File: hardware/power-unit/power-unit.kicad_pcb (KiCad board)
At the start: 2 copper layers, 114 x 80 mm, 19 parts, among them J1 VCC, J2 PWR Switch, J3 5V out, J4 Rear LED data, J5 LED left, J6 LED right, K1 G5LE-1

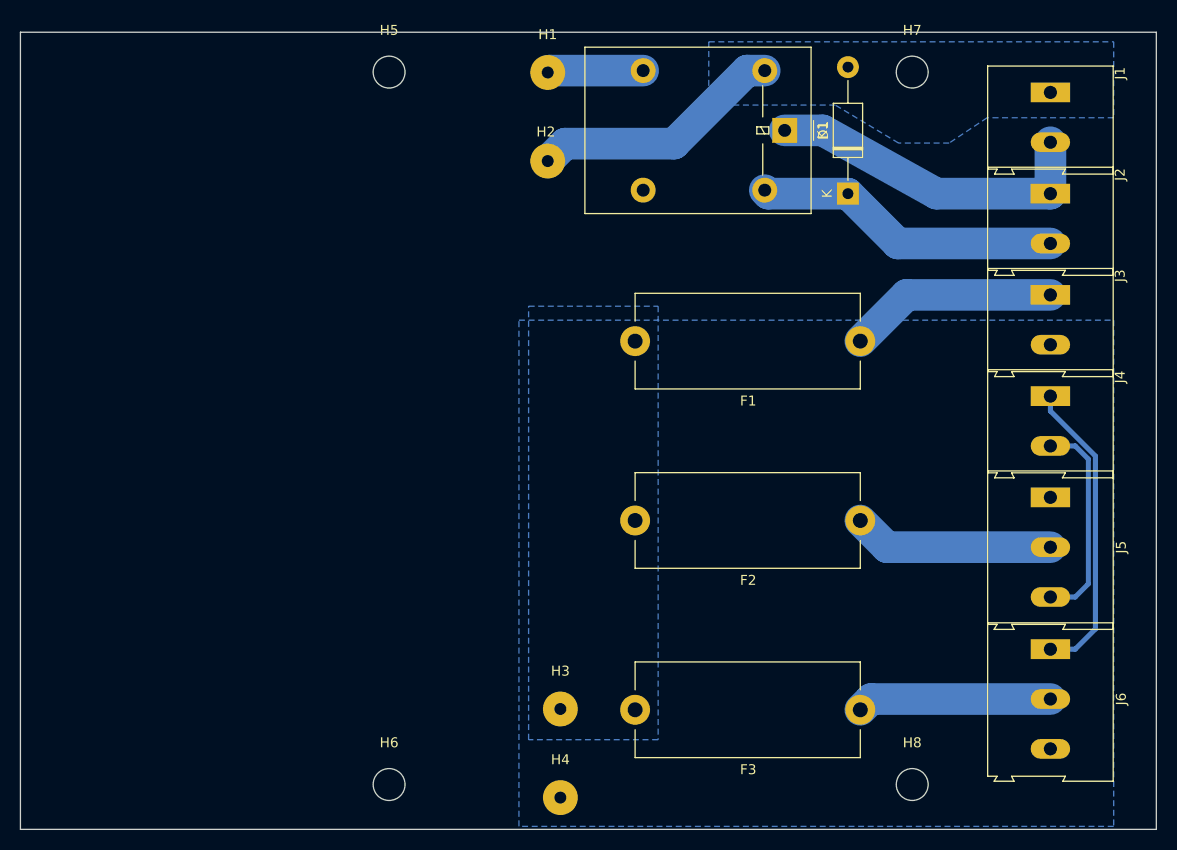
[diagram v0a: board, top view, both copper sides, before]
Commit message: Update power unit pcb
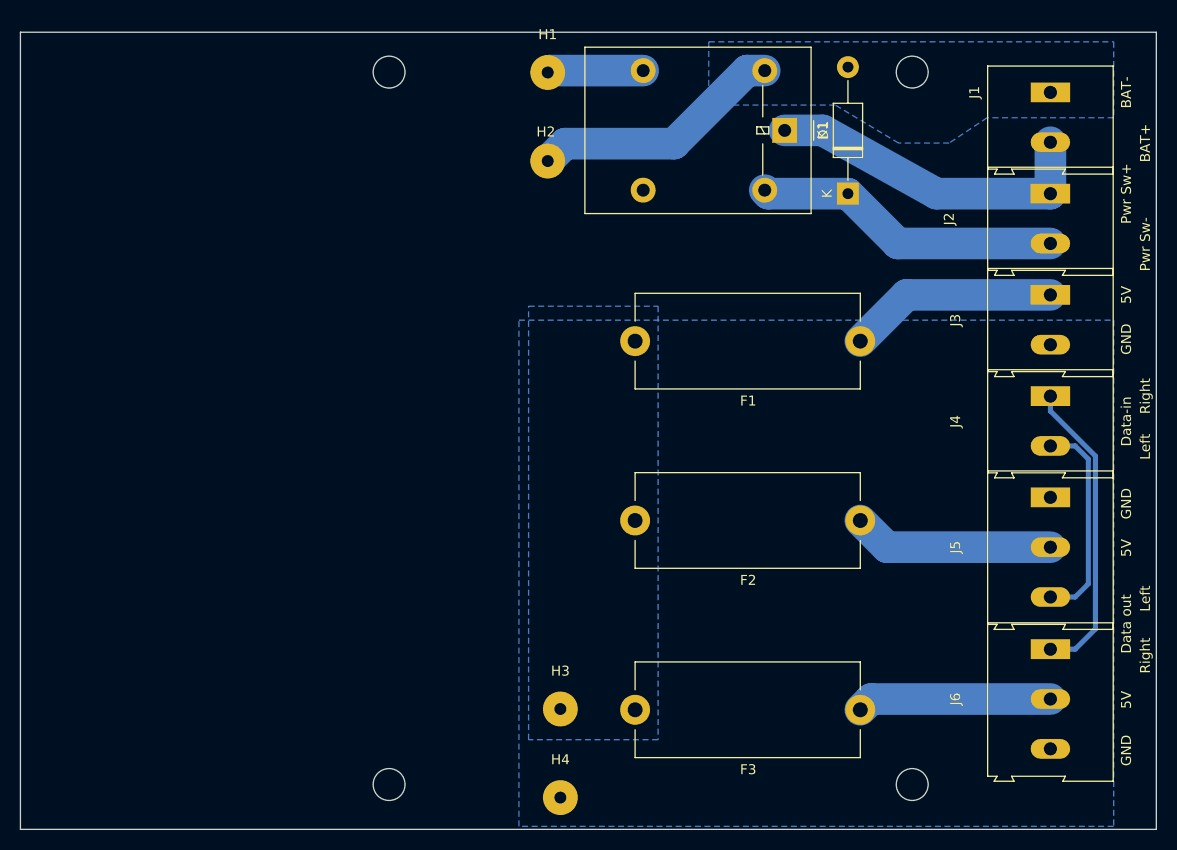
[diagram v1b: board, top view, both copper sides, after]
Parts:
- J1: value VCC -> VCC 12V
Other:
- board text added: "5V"
- board text added: "BAT+"
- board text added: "BAT-"
- board text added: "Data out"
- board text added: "Data-in"
- board text added: "GND"
- board text added: "Left"
- board text added: "Pwr Sw+"
- board text added: "Pwr Sw-"
- board text added: "Right"
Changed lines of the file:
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@@
   (general
     (thickness 1.6)
-    (drawings 16)
+    (drawings 32)
     (tracks 30)
     (zones 0)
@@
   )
   (setup
-    (last_trace_width 0.508)
+    (last_trace_width 0.25)
     (user_trace_width 0.508)
     (user_trace_width 3.175)
@@
     (visible_elements 7FFFEFFF)
     (pcbplotparams
-      (layerselection 0x010fc_ffffffff)
+      (layerselection 0x21060_fffffffe)
       (usegerberextensions false)
       (usegerberattributes false)
       (usegerberadvancedattributes false)
       (creategerberjobfile false)
-      (excludeedgelayer true)
+      (excludeedgelayer false)
       (linewidth 0.100000)
       (plotframeref false)
@@
       (padsonsilk false)
       (subtractmaskfromsilk false)
-      (outputformat 1)
+      (outputformat 4)
       (mirror false)
-      (drillshape 1)
+      (drillshape 2)
       (scaleselection 1)
-      (outputdirectory ""))
+      (outputdirectory "c:/Users/gohol/OneDrive/Documents/Cargo bike lights/power-unit/"))
   )
   (net 0 "")
@@
     (clearance 2.032)
     (attr virtual)
-    (fp_text reference H8 (at 0 -4.2) (layer F.SilkS)
-      (effects (font (size 1 1) (thickness 0.15)))
-    )
-    (fp_text value MountingHole (at 0 4.2) (layer F.Fab)
+    (fp_text reference H8 (at 0 -4.2) (layer F.SilkS) hide
+      (effects (font (size 1 1) (thickness 0.15)))
+    )
+    (fp_text value MountingHole (at 0 4.2) (layer F.Fab) hide
       (effects (font (size 1 1) (thickness 0.15)))
     )
@@
     (clearance 2.54)
     (attr virtual)
-    (fp_text reference H7 (at 0 -4.2) (layer F.SilkS)
-      (effects (font (size 1 1) (thickness 0.15)))
-    )
-    (fp_text value MountingHole (at 0 4.2) (layer F.Fab)
+    (fp_text reference H7 (at 0 -4.2) (layer F.SilkS) hide
+      (effects (font (size 1 1) (thickness 0.15)))
+    )
+    (fp_text value MountingHole (at 0 4.2) (layer F.Fab) hide
       (effects (font (size 1 1) (thickness 0.15)))
     )
@@
     (tags "mounting hole 3.2mm no annular m3")
     (attr virtual)
-    (fp_text reference H6 (at 0 -4.2) (layer F.SilkS)
-      (effects (font (size 1 1) (thickness 0.15)))
-    )
-    (fp_text value MountingHole (at 0 4.2) (layer F.Fab)
+    (fp_text reference H6 (at 0 -4.2) (layer F.SilkS) hide
+      (effects (font (size 1 1) (thickness 0.15)))
+    )
+    (fp_text value MountingHole (at 0 4.2) (layer F.Fab) hide
       (effects (font (size 1 1) (thickness 0.15)))
     )
@@
     (tags "mounting hole 3.2mm no annular m3")
     (attr virtual)
-    (fp_text reference H5 (at 0 -4.2) (layer F.SilkS)
-      (effects (font (size 1 1) (thickness 0.15)))
-    )
-    (fp_text value MountingHole (at 0 4.2) (layer F.Fab)
+    (fp_text reference H5 (at 0 -4.2) (layer F.SilkS) hide
+      (effects (font (size 1 1) (thickness 0.15)))
+    )
+    (fp_text value MountingHole (at 0 4.2) (layer F.Fab) hide
       (effects (font (size 1 1) (thickness 0.15)))
     )
@@
     (descr "Altech AK300 terminal block, pitch 5.0mm, 45 degree angled, see http://www.mouser.com/ds/2/16/PCBMETRC-24178.pdf")
     (tags "Altech AK300 terminal block pitch 5.0mm")
-    (fp_text reference J1 (at -1.92 -6.99 90) (layer F.SilkS)
-      (effects (font (size 1 1) (thickness 0.15)))
-    )
-    (fp_text value VCC (at 2.78 7.75 90) (layer F.Fab)
+    (fp_text reference J1 (at 0 7.62 90) (layer F.SilkS)
+      (effects (font (size 1 1) (thickness 0.15)))
+    )
+    (fp_text value "VCC 12V" (at 2.78 7.75 90) (layer F.Fab)
       (effects (font (size 1 1) (thickness 0.15)))
     )
@@
     (descr "Altech AK300 terminal block, pitch 5.0mm, 45 degree angled, see http://www.mouser.com/ds/2/16/PCBMETRC-24178.pdf")
     (tags "Altech AK300 terminal block pitch 5.0mm")
-    (fp_text reference J2 (at -1.92 -6.99 90) (layer F.SilkS)
+    (fp_text reference J2 (at 2.54 10.16 90) (layer F.SilkS)
       (effects (font (size 1 1) (thickness 0.15)))
     )
@@
     (descr "Altech AK300 terminal block, pitch 5.0mm, 45 degree angled, see http://www.mouser.com/ds/2/16/PCBMETRC-24178.pdf")
     (tags "Altech AK300 terminal block pitch 5.0mm")
-    (fp_text reference J3 (at -1.92 -6.99 90) (layer F.SilkS)
+    (fp_text reference J3 (at 2.54 9.525 90) (layer F.SilkS)
       (effects (font (size 1 1) (thickness 0.15)))
     )
@@
     (descr "Altech AK300 terminal block, pitch 5.0mm, 45 degree angled, see http://www.mouser.com/ds/2/16/PCBMETRC-24178.pdf")
     (tags "Altech AK300 terminal block pitch 5.0mm")
-    (fp_text reference J4 (at -1.92 -6.99 90) (layer F.SilkS)
+    (fp_text reference J4 (at 2.54 9.525 90) (layer F.SilkS)
       (effects (font (size 1 1) (thickness 0.15)))
     )
@@
     (descr "Altech AK300 terminal block, pitch 5.0mm, 45 degree angled, see http://www.mouser.com/ds/2/16/PCBMETRC-24178.pdf")
     (tags "Altech AK300 terminal block pitch 5.0mm")
-    (fp_text reference J5 (at 5 -7.1 90) (layer F.SilkS)
+    (fp_text reference J5 (at 5 9.525 90) (layer F.SilkS)
       (effects (font (size 1 1) (thickness 0.15)))
     )
@@
     (descr "Altech AK300 terminal block, pitch 5.0mm, 45 degree angled, see http://www.mouser.com/ds/2/16/PCBMETRC-24178.pdf")
     (tags "Altech AK300 terminal block pitch 5.0mm")
-    (fp_text reference J6 (at 5 -7.1 90) (layer F.SilkS)
+    (fp_text reference J6 (at 5 9.525 90) (layer F.SilkS)
       (effects (font (size 1 1) (thickness 0.15)))
     )
@@
     )
   )
+  (gr_text Left (at 175.895 116.84 90) (layer F.SilkS)
+    (effects (font (size 1 1) (thickness 0.15)))
+  )
+  (gr_text Right (at 175.895 122.555 90) (layer F.SilkS)
+    (effects (font (size 1 1) (thickness 0.15)))
+  )
+  (gr_text Data-in (at 173.99 99.06 90) (layer F.SilkS)
+    (effects (font (size 1 1) (thickness 0.15)))
+  )
+  (gr_text "Data out" (at 173.99 119.38 90) (layer F.SilkS)
+    (effects (font (size 1 1) (thickness 0.15)))
+  )
+  (gr_text 5V (at 173.99 127 90) (layer F.SilkS)
+    (effects (font (size 1 1) (thickness 0.15)))
+  )
+  (gr_text GND (at 173.99 132.08 90) (layer F.SilkS)
+    (effects (font (size 1 1) (thickness 0.15)))
+  )
+  (gr_text GND (at 173.99 107.315 90) (layer F.SilkS)
+    (effects (font (size 1 1) (thickness 0.15)))
+  )
+  (gr_text Left (at 175.895 101.6 90) (layer F.SilkS)
+    (effects (font (size 1 1) (thickness 0.15)))
+  )
+  (gr_text Right (at 175.895 96.52 90) (layer F.SilkS)
+    (effects (font (size 1 1) (thickness 0.15)))
+  )
+  (gr_text 5V (at 173.99 111.76 90) (layer F.SilkS)
+    (effects (font (size 1 1) (thickness 0.15)))
+  )
+  (gr_text GND (at 173.99 90.805 90) (layer F.SilkS)
+    (effects (font (size 1 1) (thickness 0.15)))
+  )
+  (gr_text 5V (at 173.99 86.36 90) (layer F.SilkS)
+    (effects (font (size 1 1) (thickness 0.15)))
+  )
+  (gr_text "Pwr Sw-" (at 175.895 81.28 90) (layer F.SilkS)
+    (effects (font (size 1 1) (thickness 0.15)))
+  )
+  (gr_text "Pwr Sw+" (at 173.99 76.2 90) (layer F.SilkS)
+    (effects (font (size 1 1) (thickness 0.15)))
+  )
+  (gr_text BAT+ (at 175.895 71.12 90) (layer F.SilkS)
+    (effects (font (size 1 1) (thickness 0.15)))
+  )
+  (gr_text BAT- (at 173.99 66.04 90) (layer F.SilkS)
+    (effects (font (size 1 1) (thickness 0.15)))
+  )
   (gr_circle (center 152.5 135.5) (end 151 135.5) (layer Eco1.User) (width 0.15))
